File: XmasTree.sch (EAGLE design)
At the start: 26 parts, among them Q1 MUN5235DW1T1G, Q2 MUN5235DW1T1G, U1 MCP1640C, U2 ATtiny84A-SSU

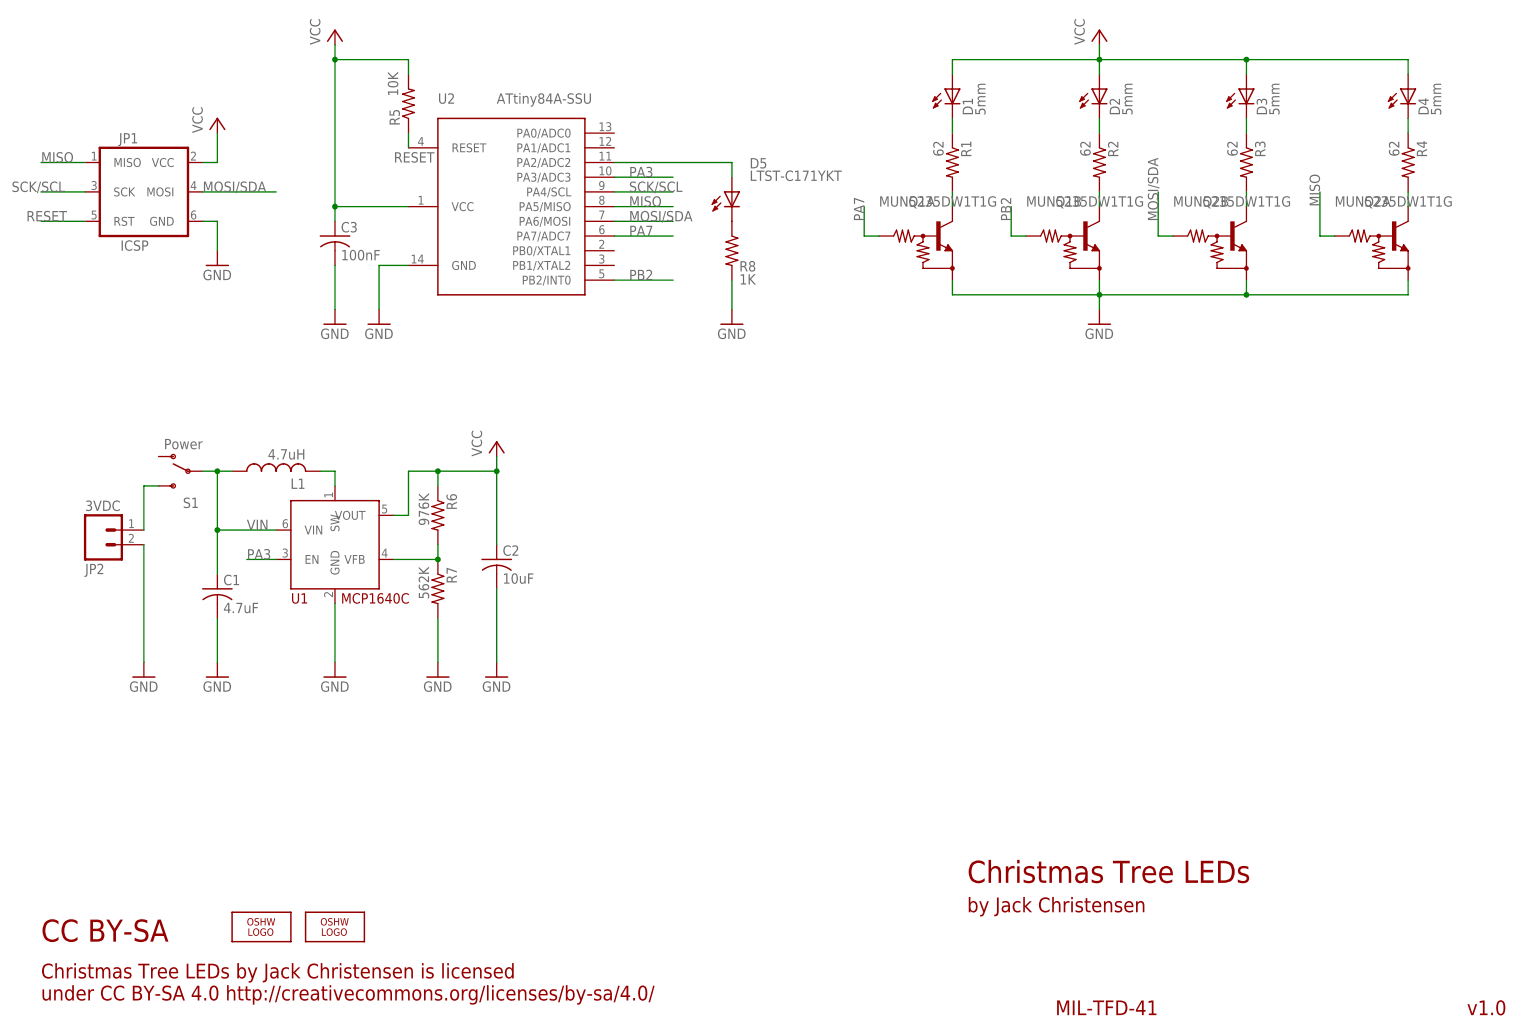
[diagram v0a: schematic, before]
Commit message: Add select button.
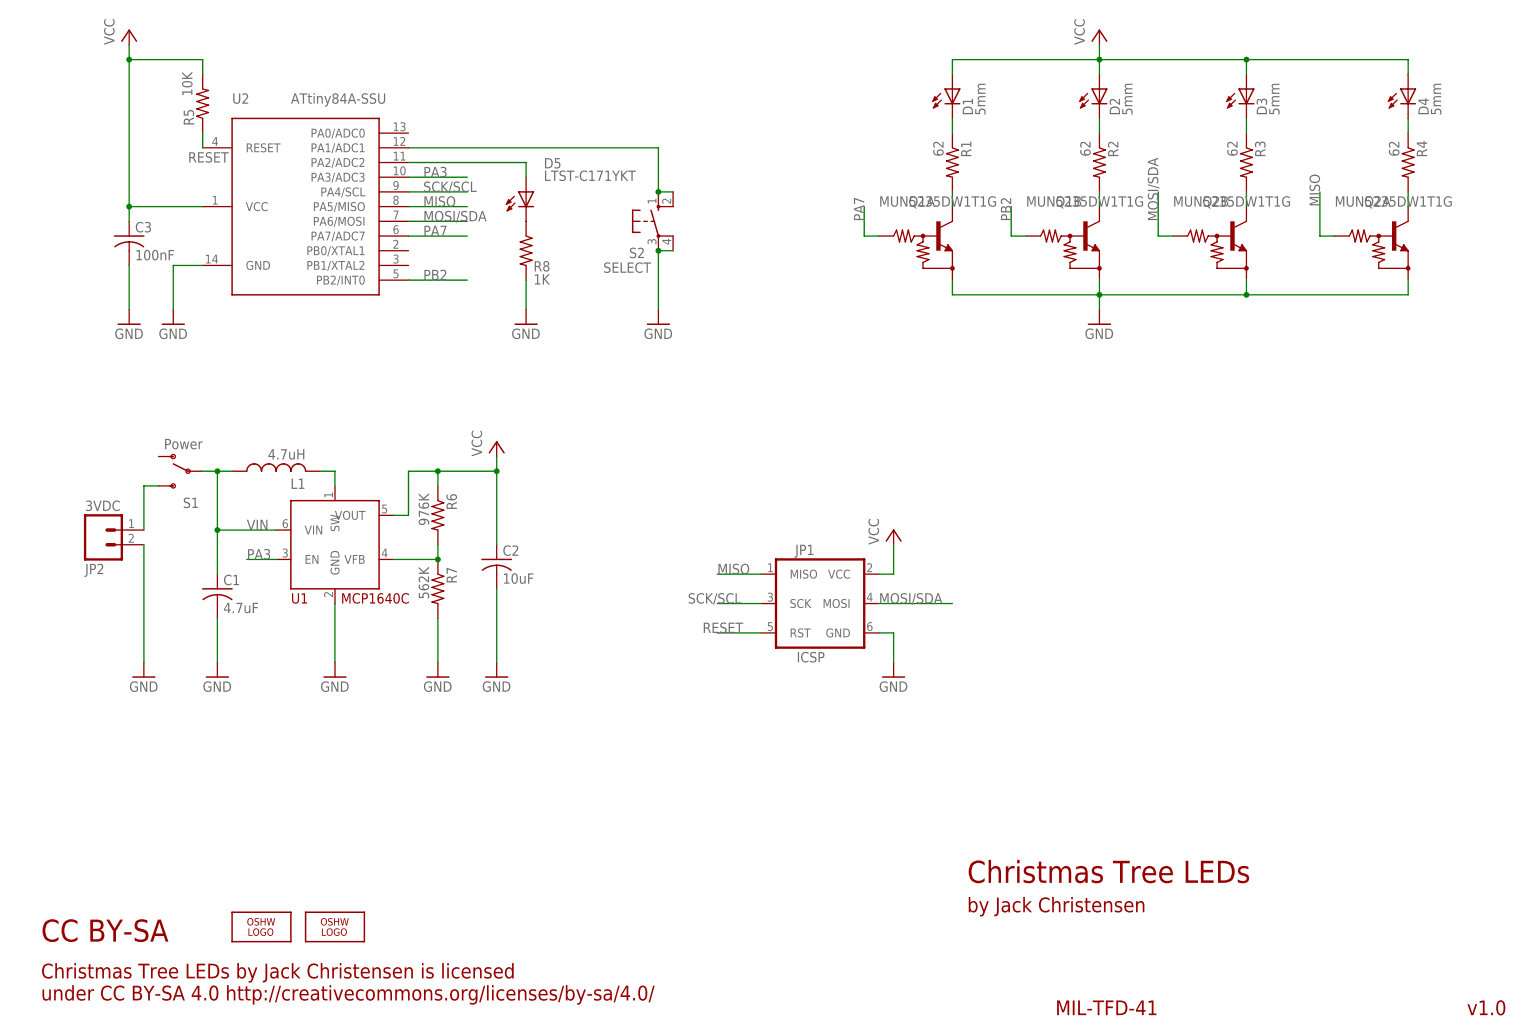
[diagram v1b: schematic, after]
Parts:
- added S2: SELECT, _jc:10-XXOCT
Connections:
- new net N$12: S2.S, S2.S1, U2.PA1/ADC1
- net GND: now also S2.P, S2.P1
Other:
- moved on the sheet: C3, D5, JP1, R5, R8, U2

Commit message: Update LED dropping resistor values.
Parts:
- R1, R2, R3, R4: value 62 -> 15
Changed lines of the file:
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@@
 <part name="Q2" library="_jc" deviceset="MUN52XX" device="SOT363" value="MUN5235DW1T1G"/>
 <part name="D1" library="_jc" deviceset="LED" device="5MM" value="5mm"/>
-<part name="R2" library="_jc" deviceset="R-US_" device="M0805" value="62"/>
+<part name="R2" library="_jc" deviceset="R-US_" device="M0805" value="15"/>
 <part name="D2" library="_jc" deviceset="LED" device="5MM" value="5mm"/>
-<part name="R1" library="_jc" deviceset="R-US_" device="M0805" value="62"/>
+<part name="R1" library="_jc" deviceset="R-US_" device="M0805" value="15"/>
 <part name="GND1" library="supply1" deviceset="GND" device=""/>
-<part name="R3" library="_jc" deviceset="R-US_" device="M0805" value="62"/>
-<part name="R4" library="_jc" deviceset="R-US_" device="M0805" value="62"/>
+<part name="R3" library="_jc" deviceset="R-US_" device="M0805" value="15"/>
+<part name="R4" library="_jc" deviceset="R-US_" device="M0805" value="15"/>
 <part name="D3" library="_jc" deviceset="LED" device="5MM" value="5mm"/>
 <part name="D4" library="_jc" deviceset="LED" device="5MM" value="5mm"/>

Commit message: Board tweaks.
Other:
- note added: "v1.1"
- note removed: "v1.0"
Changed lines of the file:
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@@
 under CC BY-SA 4.0 http://creativecommons.org/licenses/by-sa/4.0/                       </text>
 <text x="15.24" y="20.32" size="3.81" layer="94" ratio="12">CC BY-SA</text>
-<text x="261.62" y="7.62" size="2.54" layer="94" ratio="12">v1.0</text>
+<text x="261.62" y="7.62" size="2.54" layer="94" ratio="12">v1.1</text>
 <text x="190.5" y="7.62" size="2.54" layer="94" ratio="12">MIL-TFD-41</text>
 </plain>

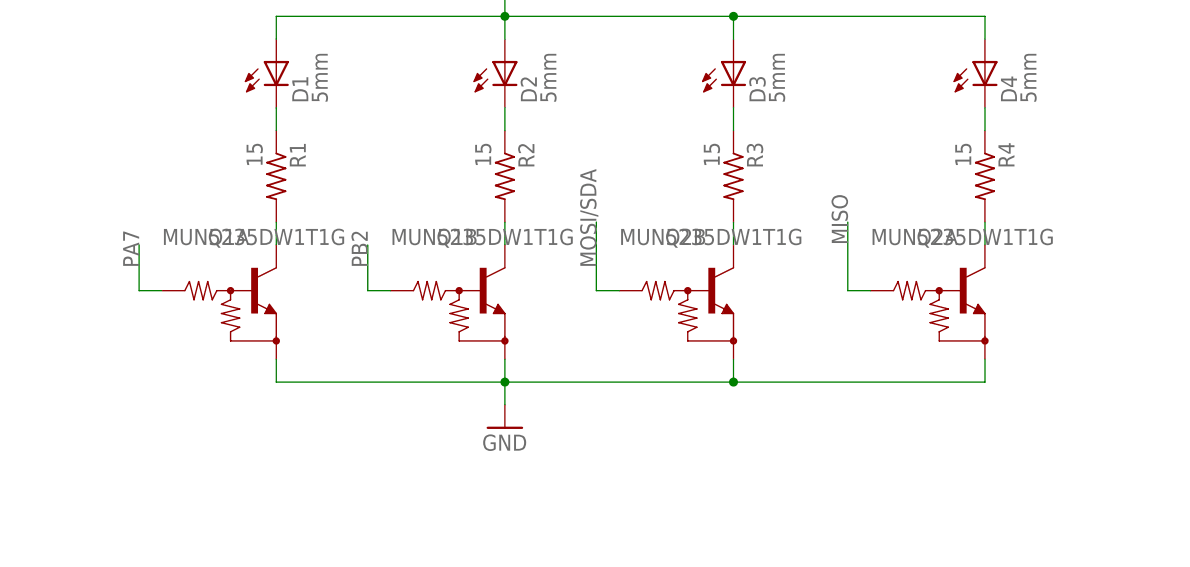
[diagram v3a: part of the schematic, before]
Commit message: Cosmetic tweaks to schematic.
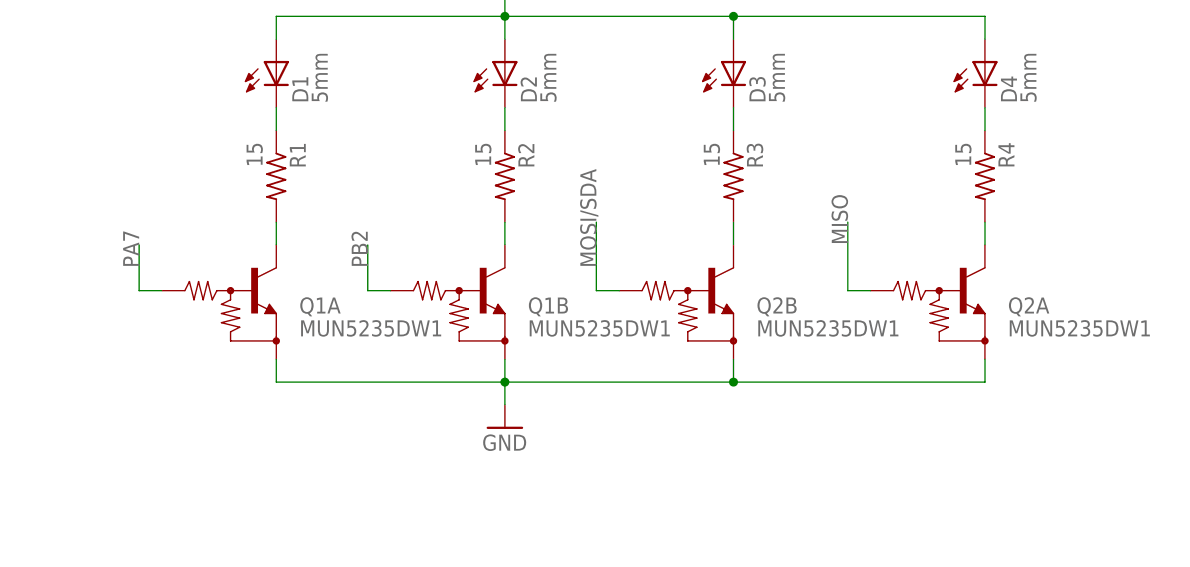
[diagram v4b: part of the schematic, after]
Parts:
- Q1, Q2: value MUN5235DW1T1G -> MUN5235DW1
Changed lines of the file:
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@@
 <part name="R5" library="_jc" deviceset="R-US_" device="M0805" value="10K"/>
 <part name="C3" library="_jc" deviceset="C-US" device="M0805" value="100nF"/>
-<part name="Q1" library="_jc" deviceset="MUN52XX" device="SOT363" value="MUN5235DW1T1G"/>
-<part name="Q2" library="_jc" deviceset="MUN52XX" device="SOT363" value="MUN5235DW1T1G"/>
+<part name="Q1" library="_jc" deviceset="MUN52XX" device="SOT363" value="MUN5235DW1"/>
+<part name="Q2" library="_jc" deviceset="MUN52XX" device="SOT363" value="MUN5235DW1"/>
 <part name="D1" library="_jc" deviceset="LED" device="5MM" value="5mm"/>
 <part name="R2" library="_jc" deviceset="R-US_" device="M0805" value="15"/>
@@
 </instance>
 <instance part="Q1" gate="A" x="170.18" y="142.24" smashed="yes">
-<attribute name="NAME" x="165.1" y="147.32" size="1.778" layer="95"/>
-<attribute name="VALUE" x="160.02" y="147.32" size="1.778" layer="96"/>
+<attribute name="NAME" x="175.26" y="139.7" size="1.778" layer="95"/>
+<attribute name="VALUE" x="175.26" y="137.16" size="1.778" layer="96"/>
 </instance>
 <instance part="Q1" gate="B" x="195.58" y="142.24" smashed="yes">
-<attribute name="NAME" x="190.5" y="147.32" size="1.778" layer="95"/>
-<attribute name="VALUE" x="185.42" y="147.32" size="1.778" layer="96"/>
+<attribute name="NAME" x="200.66" y="139.7" size="1.778" layer="95"/>
+<attribute name="VALUE" x="200.66" y="137.16" size="1.778" layer="96"/>
 </instance>
 <instance part="Q2" gate="A" x="248.92" y="142.24" smashed="yes">
-<attribute name="NAME" x="243.84" y="147.32" size="1.778" layer="95"/>
-<attribute name="VALUE" x="238.76" y="147.32" size="1.778" layer="96"/>
+<attribute name="NAME" x="254" y="139.7" size="1.778" layer="95"/>
+<attribute name="VALUE" x="254" y="137.16" size="1.778" layer="96"/>
 </instance>
 <instance part="Q2" gate="B" x="220.98" y="142.24" smashed="yes">
-<attribute name="NAME" x="215.9" y="147.32" size="1.778" layer="95"/>
-<attribute name="VALUE" x="210.82" y="147.32" size="1.778" layer="96"/>
+<attribute name="NAME" x="226.06" y="139.7" size="1.778" layer="95"/>
+<attribute name="VALUE" x="226.06" y="137.16" size="1.778" layer="96"/>
 </instance>
 <instance part="D1" gate="G$1" x="172.72" y="167.64" smashed="yes">
